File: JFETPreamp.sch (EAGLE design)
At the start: 30 parts, among them IC1 ICL7660CBA, IC2 LF356MX, IC3 LF356MX, J1 Input, J2 5V In, J3 Range Select, J4 Output

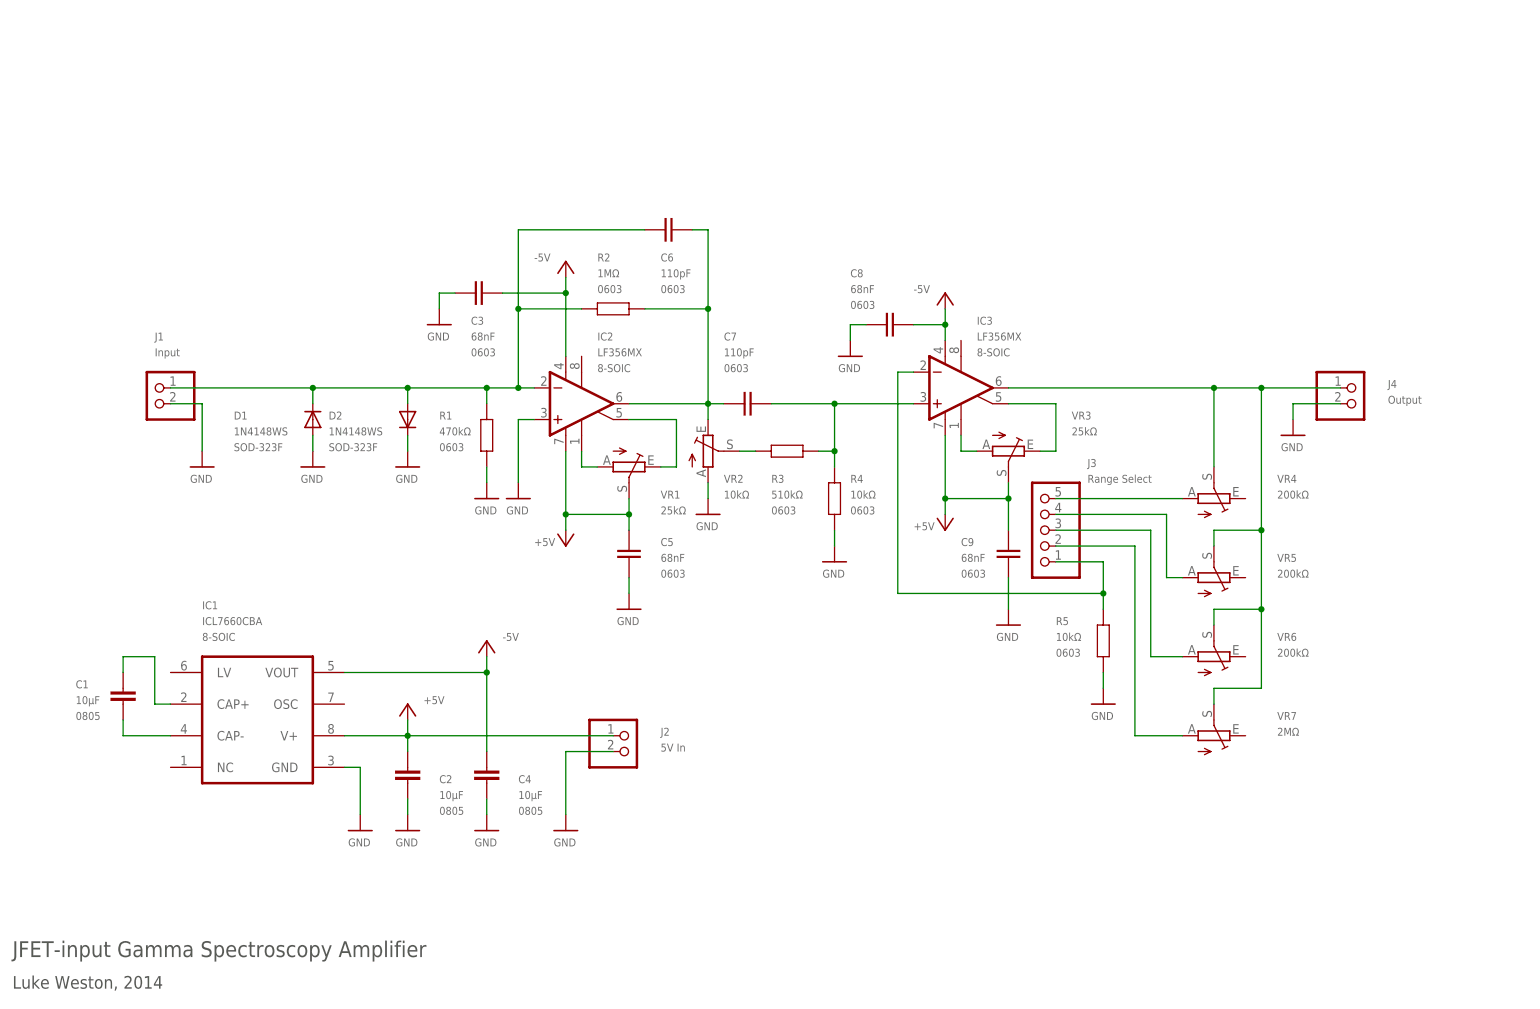
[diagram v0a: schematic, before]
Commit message: changed to single dual opamp
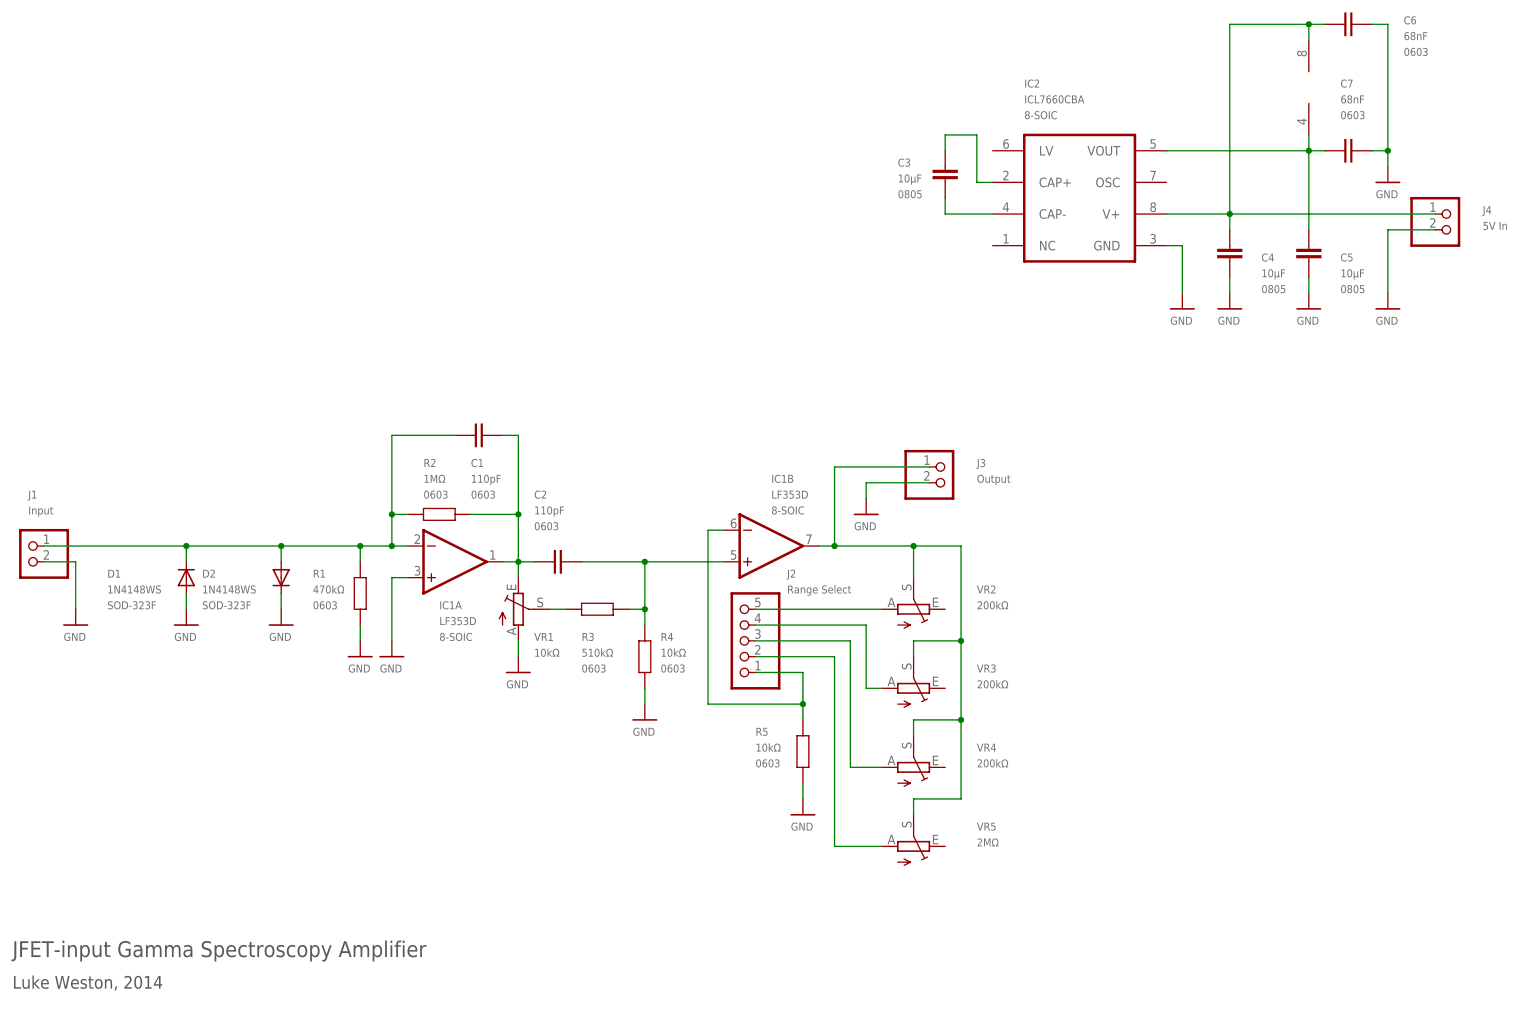
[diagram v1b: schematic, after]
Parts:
- removed C8, C9: 68nF, freetronics-luke:CAPACITOR0603
- removed IC3: LF356MX, linear:LF356D
- removed VR6: 200kΩ, pot:TRIM_EU-B25P
- removed VR7: 2MΩ, pot:TRIM_EU-B25P
- C1, C2: value 10µF -> 110pF; device rcl:C-EUC0805K -> freetronics-luke:CAPACITOR0603; PACKAGE 0805 -> 0603
- C3, C5: value 68nF -> 10µF; device freetronics-luke:CAPACITOR0603 -> rcl:C-EUC0805K; PACKAGE 0603 -> 0805
- C6, C7: value 110pF -> 68nF
- IC1: value ICL7660CBA -> LF353D; device maxim:ICL7660CSA -> linear:LF353D
- IC2: value LF356MX -> ICL7660CBA; device linear:LF356D -> maxim:ICL7660CSA
- J2: value 5V In -> Range Select; device pinhead:PINHD-1X2 -> pinhead:PINHD-1X5
- J3: value Range Select -> Output; device pinhead:PINHD-1X5 -> pinhead:PINHD-1X2
- J4: value Output -> 5V In
- VR1: value 25kΩ -> 10kΩ
- VR2: value 10kΩ -> 200kΩ
- VR3: value 25kΩ -> 200kΩ
- VR5: value 200kΩ -> 2MΩ
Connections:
- removed net +5V: C2.1, C5.2, C9.2, IC1.V+, IC2.V+, IC3.V+, J2.1, VR1.S, VR3.S
- removed net -5V: C3.2, C4.1, C8.2, IC1.VOUT, IC2.V-, IC3.V-
- removed net N$12: IC3.ON2, VR3.E
- removed net N$14: IC2.ON2, VR1.E
- net GND: now also C5.2, C6.1, C7.1, IC1A.+IN, IC2.GND, J3.2, VR1.A; no longer C2.2, C3.1, C5.1, C8.1, C9.1, IC1.GND, IC2.+IN, J2.2, VR2.A
- net N$1: now also C1.1, IC1A.-IN; no longer C6.1, IC2.-IN
- net N$10: now also J2.2, VR5.A; no longer J3.2, VR7.A
- net N$11: now also C5.1, C7.2, IC1P.V-, IC2.VOUT; no longer IC3.ON1, VR3.A
- net N$13: now also C4.1, C6.2, IC1P.V+, IC2.V+, J4.1; no longer IC2.ON1, VR1.A
- net N$15: now also C3.1, IC2.CAP+; no longer C1.1, IC1.CAP+
- net N$16: now also C3.2, IC2.CAP-; no longer C1.2, IC1.CAP-
- net N$2: now also C2.2, IC1B.+IN; no longer C7.2, IC3.+IN
- net N$3: now also C1.2, C2.1, IC1A.OUT, VR1.E; no longer C6.2, C7.1, IC2.OUT, VR2.E
- net N$4: now also IC1B.-IN, J2.1; no longer IC3.-IN, J3.1
- net N$5: now also VR1.S; no longer VR2.S
- net N$6: now also J2.5, VR2.A; no longer J3.5, VR4.A
- net N$7: now also IC1B.OUT, J3.1, VR2.S, VR3.S; no longer IC3.OUT, J4.1, VR6.S, VR7.S
- net N$8: now also J2.4, VR3.A; no longer J3.4, VR5.A
- net N$9: now also J2.3, VR4.A; no longer J3.3, VR6.A
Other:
- moved on the sheet: C4, C6, C7, D1, D2, J1, J4, R1, R2, R3, R4, R5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

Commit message: changed selector switch footprint
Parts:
- added J5: Range Select, pinhead:PINHD-1X5
- J4: value 5V In -> Pwr In
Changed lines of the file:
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@@
 <grid distance="0.1" unitdist="inch" unit="inch" style="lines" multiple="1" display="no" altdistance="0.01" altunitdist="inch" altunit="inch"/>
 <layers>
-<layer number="1" name="Top" color="4" fill="1" visible="yes" active="no"/>
-<layer number="2" name="Route2" color="1" fill="3" visible="yes" active="no"/>
-<layer number="3" name="Route3" color="4" fill="3" visible="yes" active="no"/>
-<layer number="14" name="Route14" color="1" fill="6" visible="yes" active="no"/>
-<layer number="15" name="Route15" color="4" fill="6" visible="yes" active="no"/>
-<layer number="16" name="Bottom" color="1" fill="1" visible="yes" active="no"/>
-<layer number="17" name="Pads" color="2" fill="1" visible="yes" active="no"/>
-<layer number="18" name="Vias" color="2" fill="1" visible="yes" active="no"/>
-<layer number="19" name="Unrouted" color="6" fill="1" visible="yes" active="no"/>
-<layer number="20" name="Dimension" color="15" fill="1" visible="yes" active="no"/>
-<layer number="21" name="tPlace" color="7" fill="1" visible="yes" active="no"/>
-<layer number="22" name="bPlace" color="7" fill="1" visible="yes" active="no"/>
-<layer number="23" name="tOrigins" color="15" fill="1" visible="yes" active="no"/>
-<layer number="24" name="bOrigins" color="15" fill="1" visible="yes" active="no"/>
-<layer number="25" name="tNames" color="7" fill="1" visible="yes" active="no"/>
-<layer number="26" name="bNames" color="7" fill="1" visible="yes" active="no"/>
-<layer number="27" name="tValues" color="7" fill="1" visible="yes" active="no"/>
-<layer number="28" name="bValues" color="7" fill="1" visible="yes" active="no"/>
+<layer number="1" name="Top" color="4" fill="1" visible="no" active="no"/>
+<layer number="2" name="Route2" color="1" fill="3" visible="no" active="no"/>
+<layer number="3" name="Route3" color="4" fill="3" visible="no" active="no"/>
+<layer number="14" name="Route14" color="1" fill="6" visible="no" active="no"/>
+<layer number="15" name="Route15" color="4" fill="6" visible="no" active="no"/>
+<layer number="16" name="Bottom" color="1" fill="1" visible="no" active="no"/>
+<layer number="17" name="Pads" color="2" fill="1" visible="no" active="no"/>
+<layer number="18" name="Vias" color="2" fill="1" visible="no" active="no"/>
+<layer number="19" name="Unrouted" color="6" fill="1" visible="no" active="no"/>
+<layer number="20" name="Dimension" color="15" fill="1" visible="no" active="no"/>
+<layer number="21" name="tPlace" color="7" fill="1" visible="no" active="no"/>
+<layer number="22" name="bPlace" color="7" fill="1" visible="no" active="no"/>
+<layer number="23" name="tOrigins" color="15" fill="1" visible="no" active="no"/>
+<layer number="24" name="bOrigins" color="15" fill="1" visible="no" active="no"/>
+<layer number="25" name="tNames" color="7" fill="1" visible="no" active="no"/>
+<layer number="26" name="bNames" color="7" fill="1" visible="no" active="no"/>
+<layer number="27" name="tValues" color="7" fill="1" visible="no" active="no"/>
+<layer number="28" name="bValues" color="7" fill="1" visible="no" active="no"/>
 <layer number="29" name="tStop" color="7" fill="3" visible="no" active="no"/>
 <layer number="30" name="bStop" color="7" fill="6" visible="no" active="no"/>
@@
 <layer number="35" name="tGlue" color="7" fill="4" visible="no" active="no"/>
 <layer number="36" name="bGlue" color="7" fill="5" visible="no" active="no"/>
-<layer number="37" name="tTest" color="7" fill="1" visible="yes" active="no"/>
-<layer number="38" name="bTest" color="7" fill="1" visible="yes" active="no"/>
+<layer number="37" name="tTest" color="7" fill="1" visible="no" active="no"/>
+<layer number="38" name="bTest" color="7" fill="1" visible="no" active="no"/>
 <layer number="39" name="tKeepout" color="4" fill="11" visible="no" active="no"/>
 <layer number="40" name="bKeepout" color="1" fill="11" visible="no" active="no"/>
@@
 <layer number="44" name="Drills" color="7" fill="1" visible="no" active="no"/>
 <layer number="45" name="Holes" color="7" fill="1" visible="no" active="no"/>
-<layer number="46" name="Milling" color="3" fill="1" visible="yes" active="no"/>
-<layer number="47" name="Measures" color="7" fill="1" visible="yes" active="no"/>
-<layer number="48" name="Document" color="7" fill="1" visible="yes" active="no"/>
-<layer number="49" name="Reference" color="7" fill="1" visible="yes" active="no"/>
-<layer number="50" name="dxf" color="7" fill="1" visible="yes" active="no"/>
-<layer number="51" name="tDocu" color="7" fill="1" visible="yes" active="no"/>
-<layer number="52" name="bDocu" color="7" fill="1" visible="yes" active="no"/>
-<layer number="53" name="tGND_GNDA" color="7" fill="9" visible="yes" active="no"/>
-<layer number="54" name="bGND_GNDA" color="1" fill="9" visible="yes" active="no"/>
-<layer number="56" name="wert" color="7" fill="1" visible="yes" active="no"/>
-<layer number="57" name="tCAD" color="7" fill="1" visible="yes" active="no"/>
-<layer number="60" name="p_dimension" color="6" fill="0" visible="yes" active="no"/>
-<layer number="61" name="pt_docu" color="7" fill="0" visible="yes" active="no"/>
+<layer number="46" name="Milling" color="3" fill="1" visible="no" active="no"/>
+<layer number="47" name="Measures" color="7" fill="1" visible="no" active="no"/>
+<layer number="48" name="Document" color="7" fill="1" visible="no" active="no"/>
+<layer number="49" name="Reference" color="7" fill="1" visible="no" active="no"/>
+<layer number="50" name="dxf" color="7" fill="1" visible="no" active="no"/>
+<layer number="51" name="tDocu" color="7" fill="1" visible="no" active="no"/>
+<layer number="52" name="bDocu" color="7" fill="1" visible="no" active="no"/>
+<layer number="53" name="tGND_GNDA" color="7" fill="9" visible="no" active="no"/>
+<layer number="54" name="bGND_GNDA" color="1" fill="9" visible="no" active="no"/>
+<layer number="56" name="wert" color="7" fill="1" visible="no" active="no"/>
+<layer number="57" name="tCAD" color="7" fill="1" visible="no" active="no"/>
+<layer number="60" name="p_dimension" color="6" fill="0" visible="no" active="no"/>
+<layer number="61" name="pt_docu" color="7" fill="0" visible="no" active="no"/>
 <layer number="91" name="Nets" color="2" fill="1" visible="yes" active="yes"/>
 <layer number="92" name="Busses" color="1" fill="1" visible="yes" active="yes"/>
@@
 <part name="U$15" library="freetronics-luke" deviceset="GND" device=""/>
 <part name="U$16" library="freetronics-luke" deviceset="GND" device=""/>
-<part name="J4" library="pinhead" deviceset="PINHD-1X2" device="" value="5V In"/>
+<part name="J4" library="pinhead" deviceset="PINHD-1X2" device="" value="Pwr In"/>
 <part name="U$17" library="freetronics-luke" deviceset="GND" device=""/>
 <part name="C3" library="rcl" deviceset="C-EU" device="C0805K" value="10µF">
@@
 </part>
 <part name="U$18" library="freetronics-luke" deviceset="GND" device=""/>
+<part name="J5" library="pinhead" deviceset="PINHD-1X5" device="" value="Range Select"/>
 </parts>
 <sheets>
@@
 </instance>
 <instance part="U$18" gate="G$1" x="231.14" y="139.7" rot="MR0"/>
+<instance part="J5" gate="A" x="175.26" y="71.12" smashed="yes" rot="R180">
+<attribute name="NAME" x="172.72" y="83.82" size="1.27" layer="95"/>
+<attribute name="VALUE" x="172.72" y="81.28" size="1.27" layer="96"/>
+</instance>
 </instances>
 <busses>
